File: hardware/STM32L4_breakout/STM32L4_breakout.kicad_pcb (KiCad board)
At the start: 2 copper layers, 84.8 x 91.2 mm, 72 parts, among them J1 12V IN, J10 GPIO, J12 USART1, J13 USART3, J15 3.3V, J16 5V, J17 12V, J2 SWD, J3 Conn_01x08, J4 Conn_01x06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

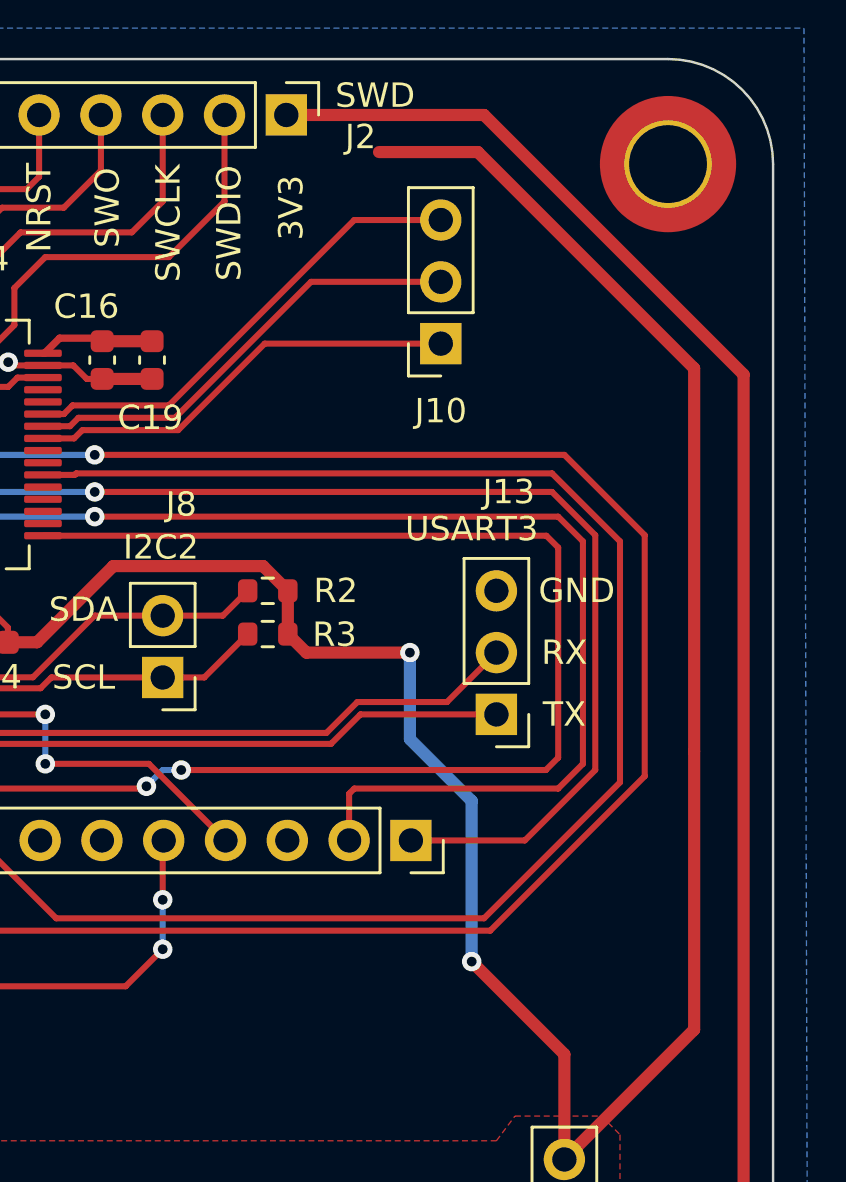
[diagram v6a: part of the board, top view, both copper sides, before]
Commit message: Update STM32L4_breakout.kicad_pcb
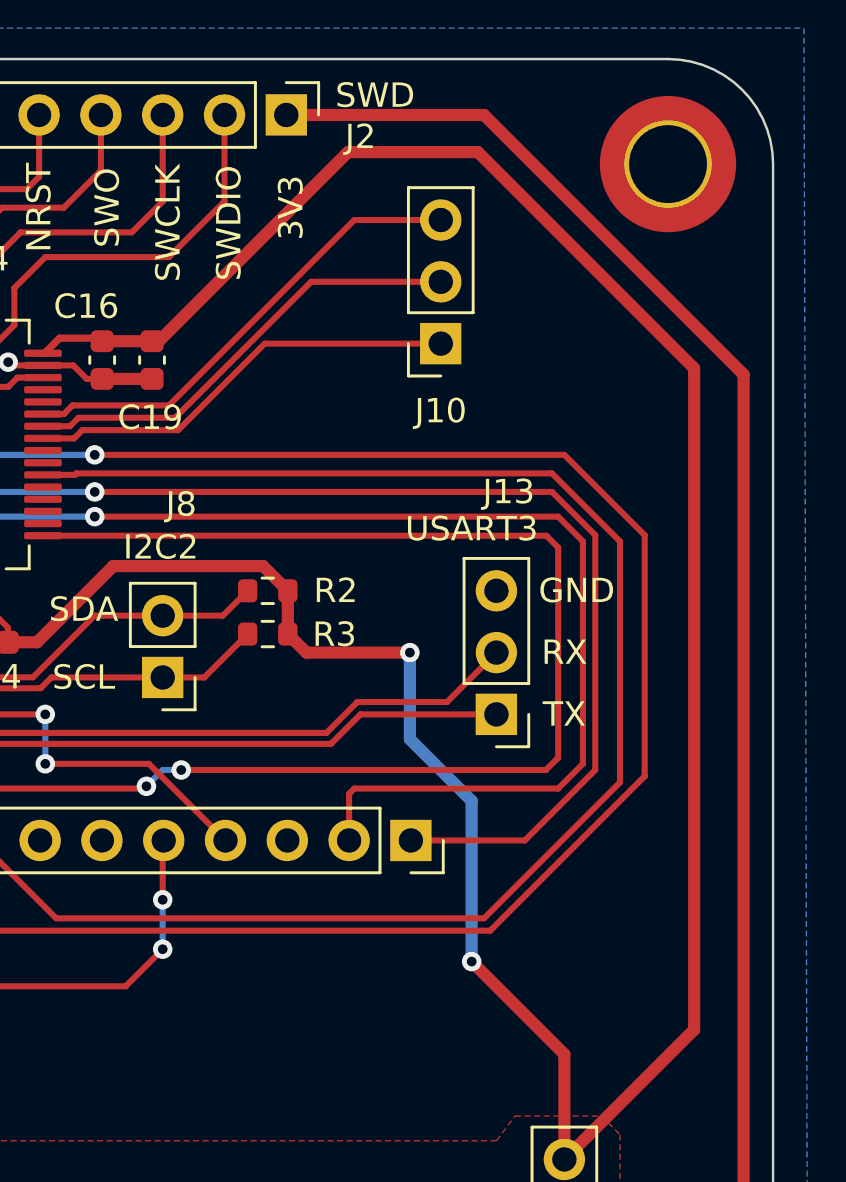
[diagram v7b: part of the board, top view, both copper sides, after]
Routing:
- net +3.3V: track 205.8 -> 218.3 mm
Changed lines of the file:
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@@
   (segment (start 144.628 95.86) (end 144.628 96.774) (width 0.25) (layer "F.Cu") (net 6))
   (segment (start 148.336 59.69) (end 148.336 58.683) (width 0.25) (layer "F.Cu") (net 6))
-  (segment (start 185.42 63.754) (end 176.53 54.864) (width 0.5) (layer "F.Cu") (net 6))
+  (segment (start 180.086 96.271) (end 185.42 90.937) (width 0.5) (layer "F.Cu") (net 6))
   (segment (start 129.286 77.025) (end 131.318 77.025) (width 0.5) (layer "F.Cu") (net 6))
   (segment (start 133.096 73.914) (end 133.096 75.438) (width 0.5) (layer "F.Cu") (net 6))
+  (segment (start 176.53 54.864) (end 171.196 54.864) (width 0.5) (layer "F.Cu") (net 6))
   (segment (start 145.838 131.419) (end 145.838 113.496) (width 0.5) (layer "F.Cu") (net 6))
-  (segment (start 185.42 90.937) (end 185.42 79.502) (width 0.5) (layer "F.Cu") (net 6))
   (segment (start 173.736 75.438) (end 169.481 75.438) (width 0.5) (layer "F.Cu") (net 6))
   (segment (start 180.086 96.271) (end 180.086 91.948) (width 0.5) (layer "F.Cu") (net 6))
@@
   (segment (start 131.572 89.408) (end 133.35 91.186) (width 0.25) (layer "F.Cu") (net 6))
   (segment (start 169.481 75.438) (end 168.719 74.676) (width 0.5) (layer "F.Cu") (net 6))
+  (segment (start 185.42 63.754) (end 176.53 54.864) (width 0.5) (layer "F.Cu") (net 6))
   (segment (start 145.838 113.496) (end 147.828 111.506) (width 0.5) (layer "F.Cu") (net 6))
   (segment (start 161.544 71.882) (end 158.412 75.014) (width 0.5) (layer "F.Cu") (net 6))
   (segment (start 133.35 73.66) (end 133.096 73.914) (width 0.5) (layer "F.Cu") (net 6))
   (segment (start 135.382 69.85) (end 134.62 70.612) (width 0.5) (layer "F.Cu") (net 6))
+  (segment (start 163.421 62.639) (end 163.138 62.639) (width 0.5) (layer "F.Cu") (net 6))
   (segment (start 158.412 75.014) (end 157.213 75.014) (width 0.5) (layer "F.Cu") (net 6))
   (segment (start 139.428 71.2855) (end 139.428 70.594) (width 0.5) (layer "F.Cu") (net 6))
   (segment (start 158.718 63.134) (end 159.338 62.514) (width 0.3) (layer "F.Cu") (net 6))
   (segment (start 129.032 87.439) (end 131.572 87.439) (width 0.25) (layer "F.Cu") (net 6))
-  (segment (start 180.086 96.271) (end 185.42 90.937) (width 0.5) (layer "F.Cu") (net 6))
-  (segment (start 176.53 54.864) (end 172.466 54.864) (width 0.5) (layer "F.Cu") (net 6))
   (segment (start 133.096 75.438) (end 131.509 77.025) (width 0.5) (layer "F.Cu") (net 6))
   (segment (start 168.719 74.676) (end 168.719 72.898) (width 0.5) (layer "F.Cu") (net 6))
@@
   (segment (start 149.228 61.209) (end 149.228 60.582) (width 0.25) (layer "F.Cu") (net 6))
   (segment (start 133.35 91.186) (end 139.954 91.186) (width 0.25) (layer "F.Cu") (net 6))
+  (segment (start 171.196 54.864) (end 163.421 62.639) (width 0.5) (layer "F.Cu") (net 6))
   (segment (start 149.228 60.582) (end 148.336 59.69) (width 0.25) (layer "F.Cu") (net 6))
   (segment (start 168.719 72.898) (end 167.703 71.882) (width 0.5) (layer "F.Cu") (net 6))
@@
   (segment (start 131.572 87.439) (end 131.572 89.408) (width 0.25) (layer "F.Cu") (net 6))
   (segment (start 138.684 69.85) (end 135.382 69.85) (width 0.5) (layer "F.Cu") (net 6))
-  (segment (start 185.42 79.502) (end 185.42 63.754) (width 0.5) (layer "F.Cu") (net 6))
   (segment (start 167.703 71.882) (end 161.544 71.882) (width 0.5) (layer "F.Cu") (net 6))
   (segment (start 147.828 111.506) (end 148.336 110.998) (width 0.5) (layer "F.Cu") (net 6))
+  (segment (start 185.42 90.937) (end 185.42 63.754) (width 0.5) (layer "F.Cu") (net 6))
   (segment (start 128.841 87.439) (end 129.032 87.439) (width 0.5) (layer "F.Cu") (net 6))
   (segment (start 157.213 74.409) (end 157.213 75.014) (width 0.25) (layer "F.Cu") (net 6))

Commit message: Update STM32L4_breakout.kicad_pcb
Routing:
- net +3.3V: track 218.3 -> 170.7 mm
- net CARDCS_5V: track 64.8 -> 57.2 mm
- net /ARD_3V3A: track 7.38 -> 6.33 mm, vias 2 -> 0
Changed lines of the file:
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@@
   (segment (start 156.728 73.924) (end 157.213 74.409) (width 0.25) (layer "F.Cu") (net 6))
   (segment (start 156.728 72.559) (end 156.728 73.924) (width 0.25) (layer "F.Cu") (net 6))
-  (segment (start 113.502 72.1) (end 128.841 87.439) (width 0.5) (layer "F.Cu") (net 6))
   (segment (start 150.228 73.399685) (end 150.622 73.793685) (width 0.25) (layer "F.Cu") (net 6))
   (segment (start 150.622 73.793685) (end 150.622 74.519) (width 0.25) (layer "F.Cu") (net 6))
@@
   (segment (start 148.818 56.226) (end 148.818 58.201) (width 0.5) (layer "F.Cu") (net 6))
   (segment (start 148.336 96.962) (end 147.828 96.454) (width 0.5) (layer "F.Cu") (net 6))
-  (segment (start 131.572 89.408) (end 133.35 91.186) (width 0.25) (layer "F.Cu") (net 6))
   (segment (start 169.481 75.438) (end 168.719 74.676) (width 0.5) (layer "F.Cu") (net 6))
   (segment (start 185.42 63.754) (end 176.53 54.864) (width 0.5) (layer "F.Cu") (net 6))
@@
   (segment (start 139.428 71.2855) (end 139.428 70.594) (width 0.5) (layer "F.Cu") (net 6))
   (segment (start 158.718 63.134) (end 159.338 62.514) (width 0.3) (layer "F.Cu") (net 6))
-  (segment (start 129.032 87.439) (end 131.572 87.439) (width 0.25) (layer "F.Cu") (net 6))
   (segment (start 133.096 75.438) (end 131.509 77.025) (width 0.5) (layer "F.Cu") (net 6))
   (segment (start 168.719 74.676) (end 168.719 72.898) (width 0.5) (layer "F.Cu") (net 6))
@@
   (segment (start 180.086 91.948) (end 176.276 88.138) (width 0.5) (layer "F.Cu") (net 6))
   (segment (start 149.228 61.209) (end 149.228 60.582) (width 0.25) (layer "F.Cu") (net 6))
-  (segment (start 133.35 91.186) (end 139.954 91.186) (width 0.25) (layer "F.Cu") (net 6))
   (segment (start 171.196 54.864) (end 163.421 62.639) (width 0.5) (layer "F.Cu") (net 6))
   (segment (start 149.228 60.582) (end 148.336 59.69) (width 0.25) (layer "F.Cu") (net 6))
   (segment (start 168.719 72.898) (end 167.703 71.882) (width 0.5) (layer "F.Cu") (net 6))
-  (segment (start 107.823 72.1) (end 113.502 72.1) (width 0.5) (layer "F.Cu") (net 6))
-  (segment (start 131.572 87.439) (end 131.572 89.408) (width 0.25) (layer "F.Cu") (net 6))
   (segment (start 138.684 69.85) (end 135.382 69.85) (width 0.5) (layer "F.Cu") (net 6))
   (segment (start 167.703 71.882) (end 161.544 71.882) (width 0.5) (layer "F.Cu") (net 6))
@@
   (segment (start 157.238 74.989) (end 157.213 75.014) (width 0.3) (layer "F.Cu") (net 6))
   (segment (start 163.138 62.639) (end 161.088 62.639) (width 0.5) (layer "F.Cu") (net 6))
-  (segment (start 139.954 91.186) (end 144.628 95.86) (width 0.25) (layer "F.Cu") (net 6))
   (via (at 173.736 75.438) (size 0.8) (drill 0.4) (layers "F.Cu" "B.Cu") (net 6))
   (via (at 176.276 88.138) (size 0.8) (drill 0.4) (layers "F.Cu" "B.Cu") (net 6))
@@
   (segment (start 140.208 78.486) (end 139.234 79.46) (width 0.25) (layer "F.Cu") (net 27))
   (segment (start 139.234 79.46) (end 139.234 83.159) (width 0.25) (layer "F.Cu") (net 27))
-  (segment (start 134.874 82.439) (end 134.154 83.159) (width 0.5) (layer "F.Cu") (net 28))
-  (segment (start 134.62 77.47) (end 133.604 78.486) (width 0.5) (layer "F.Cu") (net 28))
-  (segment (start 134.62 77.025) (end 134.62 77.47) (width 0.5) (layer "F.Cu") (net 28))
-  (segment (start 134.874 79.756) (end 134.874 82.439) (width 0.5) (layer "F.Cu") (net 28))
-  (via (at 133.604 78.486) (size 0.8) (drill 0.4) (layers "F.Cu" "B.Cu") (net 28))
-  (via (at 134.874 79.756) (size 0.8) (drill 0.4) (layers "F.Cu" "B.Cu") (net 28))
-  (segment (start 133.604 78.486) (end 134.874 79.756) (width 0.5) (layer "B.Cu") (net 28))
+  (segment (start 134.62 77.025) (end 134.154 77.491) (width 0.5) (layer "F.Cu") (net 28))
+  (segment (start 134.154 77.491) (end 134.154 83.159) (width 0.5) (layer "F.Cu") (net 28))
   (segment (start 151.13 55.118) (end 144.018 55.118) (width 0.25) (layer "F.Cu") (net 29))
   (segment (start 150.228 61.209) (end 150.228 59.83) (width 0.25) (layer "F.Cu") (net 29))
@@
   (segment (start 147.32 71.882) (end 147.32 74.168) (width 0.25) (layer "F.Cu") (net 35))
   (segment (start 147.32 74.168) (end 146.304 75.184) (width 0.25) (layer "F.Cu") (net 35))
-  (segment (start 132.842 80.518) (end 136.652 76.708) (width 0.25) (layer "F.Cu") (net 35))
+  (segment (start 144.601396 86.048) (end 145.871396 87.318) (width 0.25) (layer "F.Cu") (net 35))
   (segment (start 149.228 72.559) (end 149.228 72.52) (width 0.25) (layer "F.Cu") (net 35))
-  (segment (start 163.576 87.63) (end 162.052 89.154) (width 0.25) (layer "F.Cu") (net 35))
-  (segment (start 136.652 76.708) (end 142.748 76.708) (width 0.25) (layer "F.Cu") (net 35))
   (segment (start 163.576 85.598) (end 163.576 83.201) (width 0.25) (layer "F.Cu") (net 35))
-  (segment (start 132.842 86.614) (end 132.842 80.518) (width 0.25) (layer "F.Cu") (net 35))
+  (segment (start 135.519 85.481) (end 136.086 86.048) (width 0.25) (layer "F.Cu") (net 35))
   (segment (start 147.574 71.628) (end 147.32 71.882) (width 0.25) (layer "F.Cu") (net 35))
   (segment (start 163.576 83.201) (end 163.618 83.159) (width 0.25) (layer "F.Cu") (net 35))
-  (segment (start 142.748 76.708) (end 144.272 75.184) (width 0.25) (layer "F.Cu") (net 35))
-  (segment (start 135.382 89.154) (end 132.842 86.614) (width 0.25) (layer "F.Cu") (net 35))
+  (segment (start 139.954 76.708) (end 135.519 81.143) (width 0.25) (layer "F.Cu") (net 35))
   (segment (start 149.228 72.52) (end 148.336 71.628) (width 0.25) (layer "F.Cu") (net 35))
-  (segment (start 162.052 89.154) (end 135.382 89.154) (width 0.25) (layer "F.Cu") (net 35))
+  (segment (start 144.272 75.184) (end 142.748 76.708) (width 0.25) (layer "F.Cu") (net 35))
+  (segment (start 142.748 76.708) (end 139.954 76.708) (width 0.25) (layer "F.Cu") (net 35))
+  (segment (start 135.519 81.143) (end 135.519 85.481) (width 0.25) (layer "F.Cu") (net 35))
   (segment (start 148.336 71.628) (end 147.574 71.628) (width 0.25) (layer "F.Cu") (net 35))
+  (segment (start 145.871396 87.318) (end 163.264 87.318) (width 0.25) (layer "F.Cu") (net 35))
+  (segment (start 163.264 87.318) (end 163.576 87.63) (width 0.25) (layer "F.Cu") (net 35))
+  (segment (start 136.086 86.048) (end 144.601396 86.048) (width 0.25) (layer "F.Cu") (net 35))
   (via (at 146.304 75.184) (size 0.8) (drill 0.4) (layers "F.Cu" "B.Cu") (net 35))
   (via (at 144.272 75.184) (size 0.8) (drill 0.4) (layers "F.Cu" "B.Cu") (net 35))
